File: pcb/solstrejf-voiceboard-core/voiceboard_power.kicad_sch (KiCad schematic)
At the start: 17 parts, among them U2 L78L05_TO92, U3 L79L05_TO92

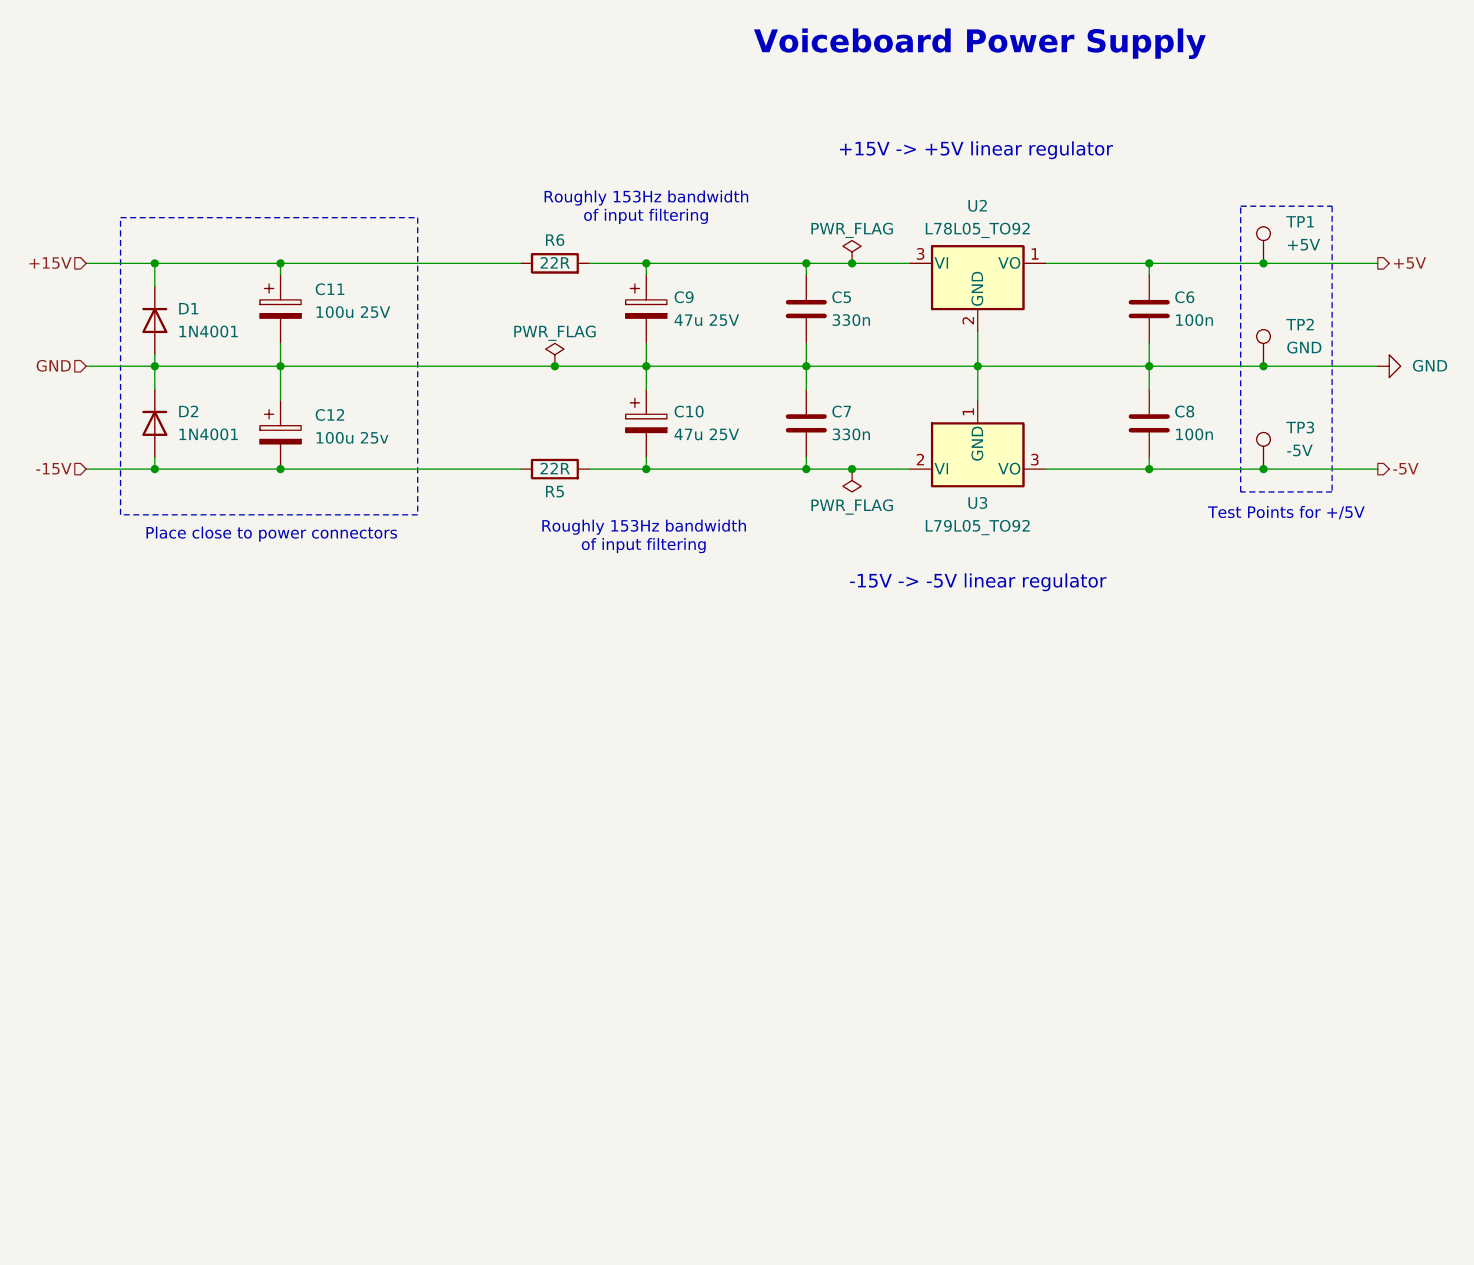
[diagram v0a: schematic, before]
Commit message: created schematic for CV circuits: PAN, VCA, and FREQ. Created a new symbol for the ONESHOT envelope generator
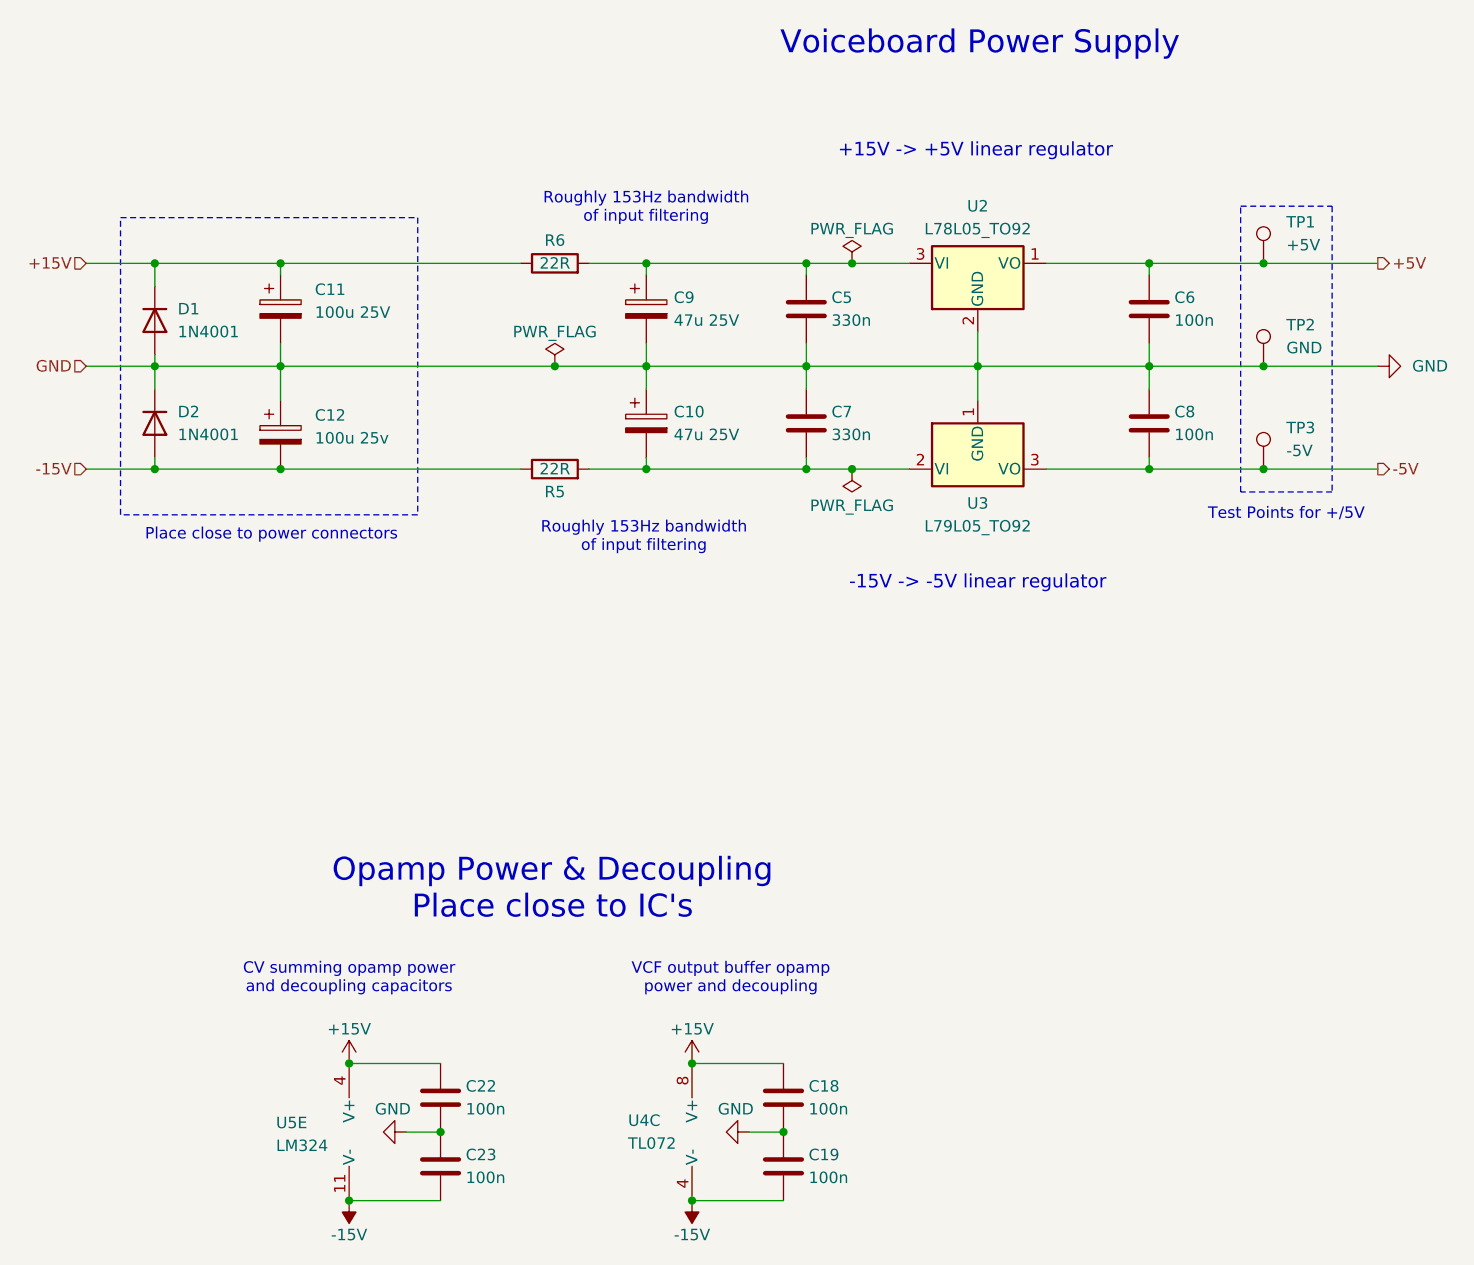
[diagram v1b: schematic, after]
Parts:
- added C18, C19, C22, C23: 100n, Capacitor_THT:C_Disc_D5.0mm_W2.5mm_P5.00mm, symbol Device:C
- added U4: TL072, Package_DIP:DIP-8_W7.62mm_Socket, symbol Amplifier_Operational:TL072
- added U5: LM324, Package_DIP:DIP-14_W7.62mm, symbol Amplifier_Operational:LM324
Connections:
- net +15V: now also C18.1, C22.1, U4.8 (V+), U5.4 (V+)
- net -15V: now also C19.2, C23.2, U4.4 (V-), U5.11 (V-)
- net GND: now also C18.2, C19.1, C22.2, C23.1
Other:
- note added: "CV summing opamp power and decoupling capacitors"
- note added: "Opamp Power & Decoupling Place close to IC's"
- note added: "VCF output buffer opamp power and decoupling"

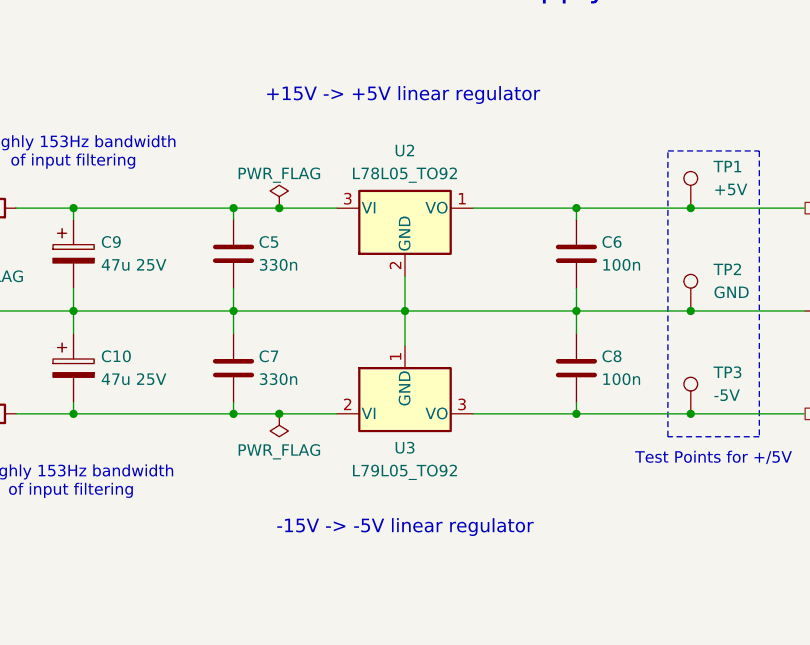
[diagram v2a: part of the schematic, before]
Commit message: Finish layout of the voice board. Included 3D renders in README.
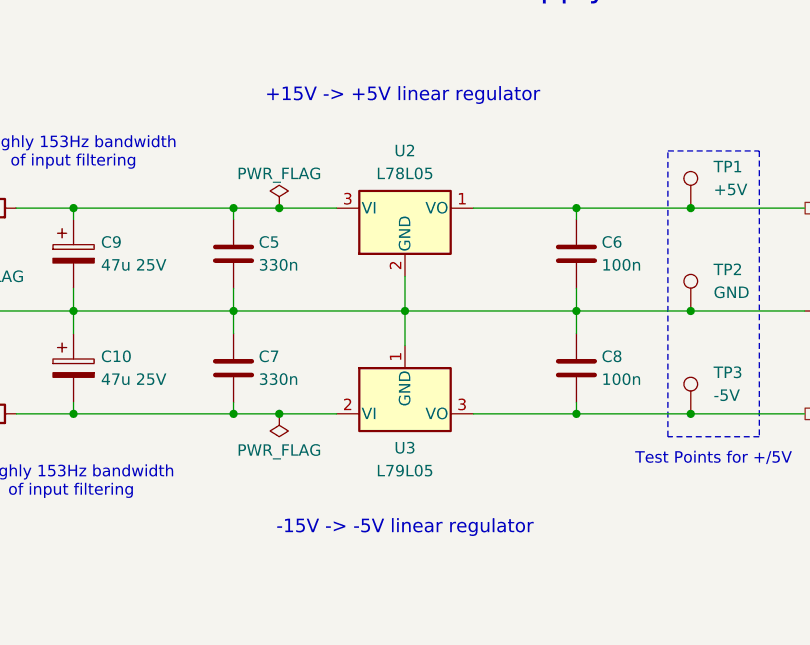
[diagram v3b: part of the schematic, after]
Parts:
- U2: value L78L05_TO92 -> L78L05
- U3: value L79L05_TO92 -> L79L05
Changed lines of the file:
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@@
 			)
 		)
-		(property "Value" "L79L05_TO92"
+		(property "Value" "L79L05"
 			(at 158.75 104.14 0)
 			(effects
@@
 			)
 		)
-		(property "Value" "L78L05_TO92"
+		(property "Value" "L78L05"
 			(at 158.75 71.12 0)
 			(effects

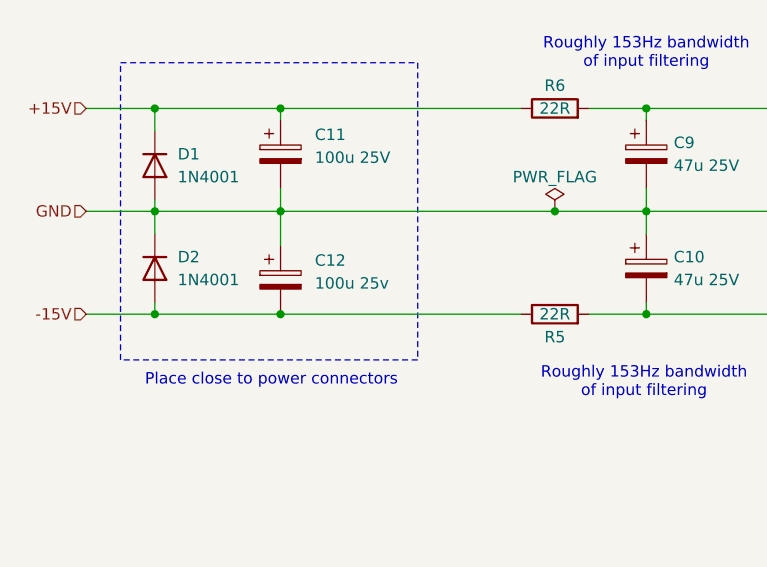
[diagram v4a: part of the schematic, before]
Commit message: Updated values of electrolytic caps on voice board to match in the ibom.
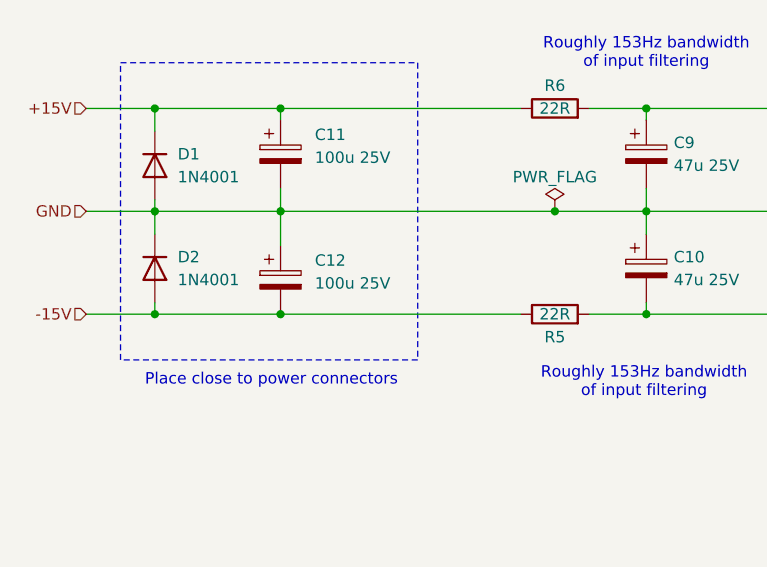
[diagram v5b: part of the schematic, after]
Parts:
- C12: value 100u 25v -> 100u 25V
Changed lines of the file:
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@@
 			)
 		)
-		(property "Value" "100u 25v"
+		(property "Value" "100u 25V"
 			(at 85.09 94.3609 0)
 			(effects

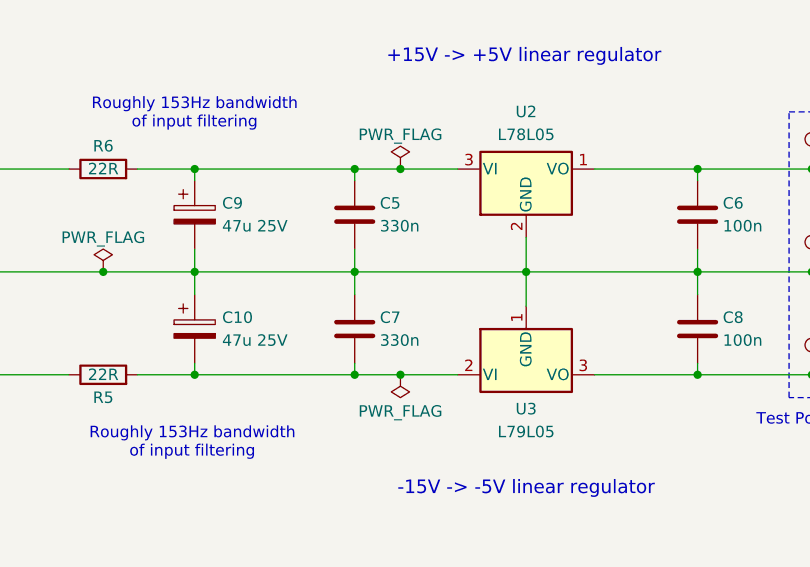
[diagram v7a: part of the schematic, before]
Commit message: Updated two capacitor values in voice board power section 330n->100n. Updated Schematic and created new IBOM.
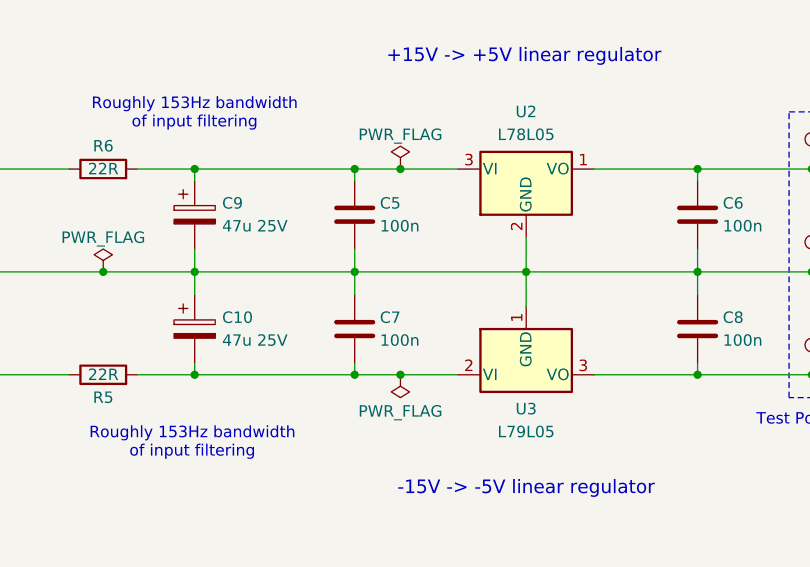
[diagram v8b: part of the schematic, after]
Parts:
- C5, C7: value 330n -> 100n
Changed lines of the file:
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@@
 	(title_block
 		(title "Soltrejf Voiceboard Power")
-		(date "2025-03-02")
+		(date "2025-03-08")
 		(rev "1.1")
 	)
@@
 			)
 		)
-		(property "Value" "330n"
+		(property "Value" "100n"
 			(at 142.494 93.98 0)
 			(effects
@@
 			)
 		)
-		(property "Value" "330n"
+		(property "Value" "100n"
 			(at 142.494 81.28 0)
 			(effects
